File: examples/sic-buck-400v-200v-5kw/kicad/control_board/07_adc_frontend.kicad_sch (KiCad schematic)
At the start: 27 parts, among them J7 J_NTC: Vishay NTCALUG01A103F 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, U15 REF3130AIDBZR, U16 LM61CIM3/NOPB

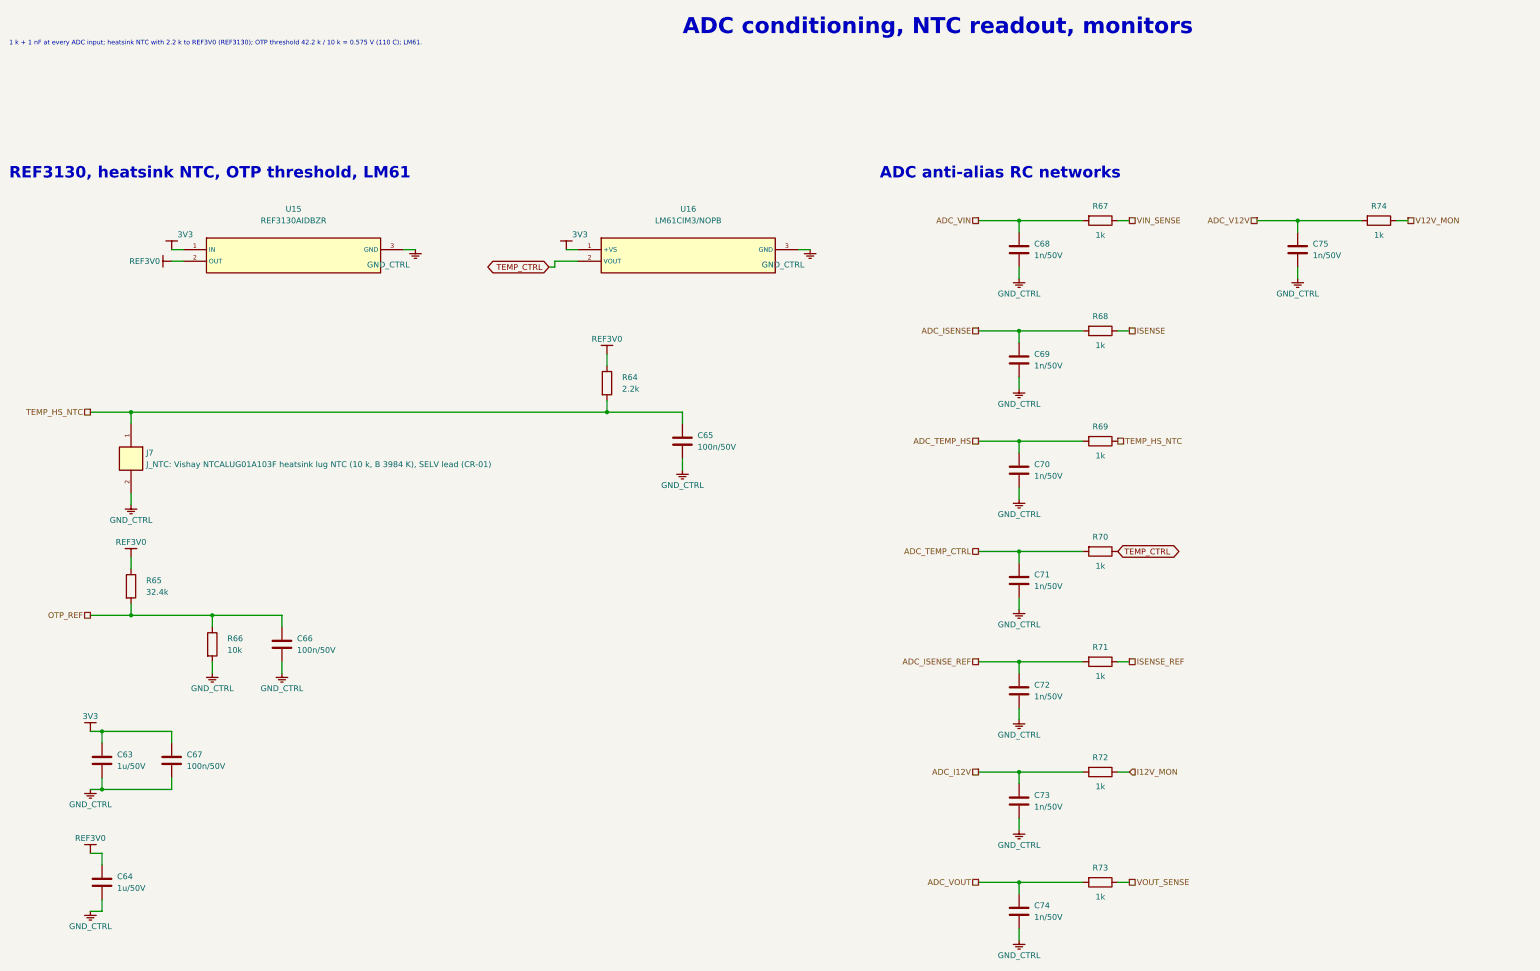
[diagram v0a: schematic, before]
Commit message: Correct sensing circuits and add verified V2.2 local bypasses
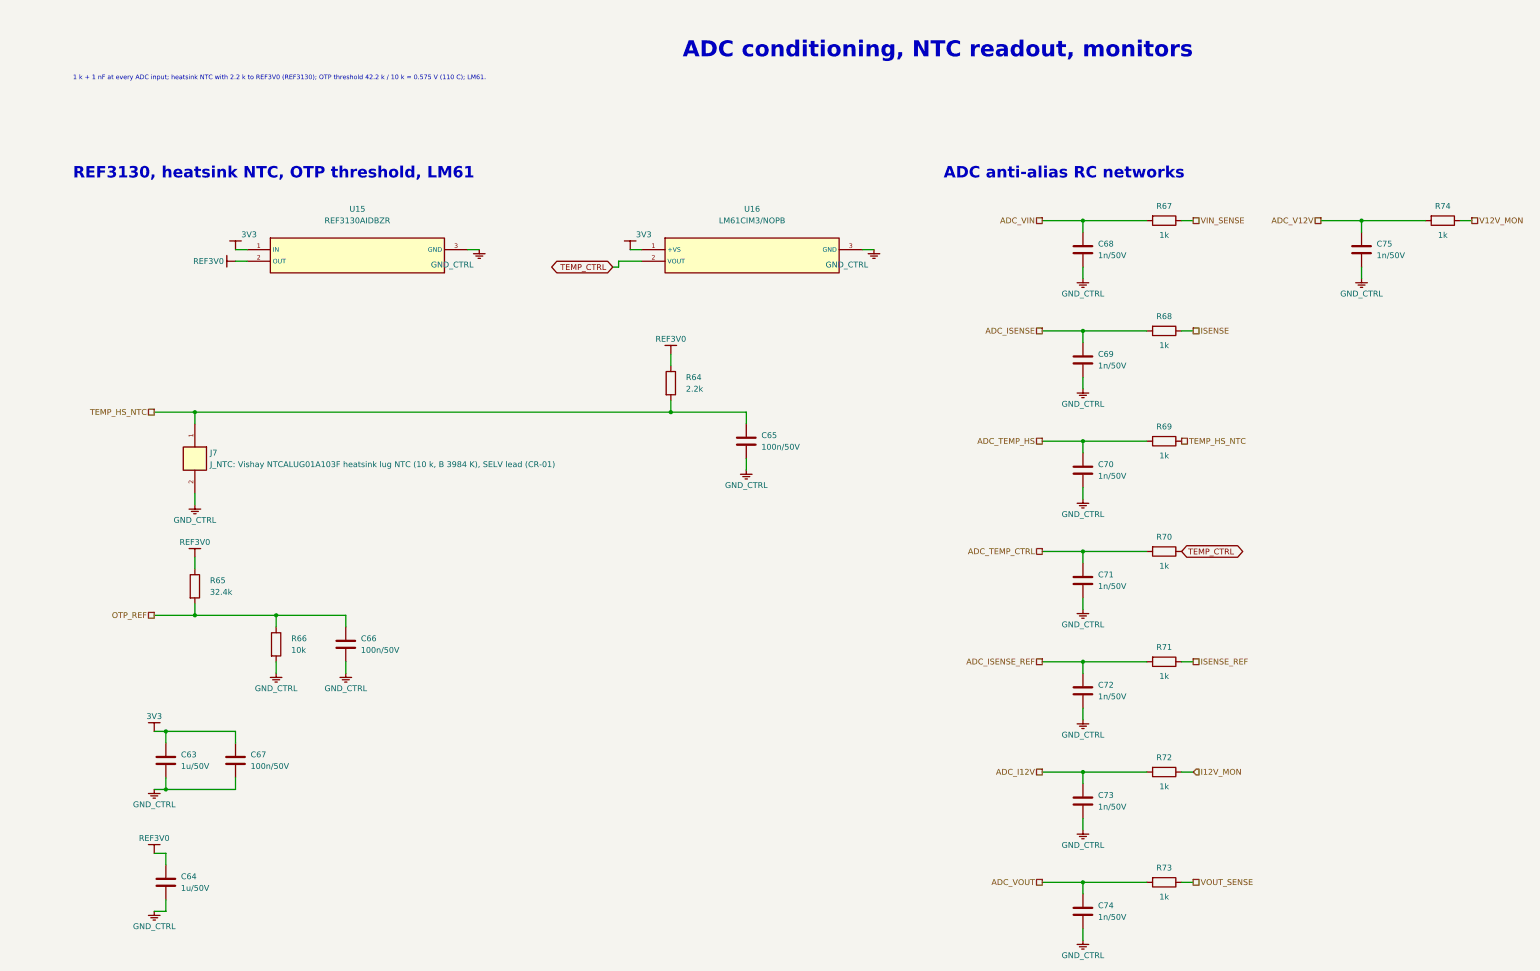
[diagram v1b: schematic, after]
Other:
- moved on the sheet: C63, C64, C65, C66, C67, C68, C69, C70, C71, C72, C73, C74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
